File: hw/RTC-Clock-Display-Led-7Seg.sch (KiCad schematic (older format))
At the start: 86 parts, among them IC1 STM8S003F3P, J1 BARREL_JACK, J4 CONN_01X04, Q1 A1015, Q10 C1815, Q2 A1015, Q3 A1015, Q4 A1015, Q5 C1815, Q6 C1815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

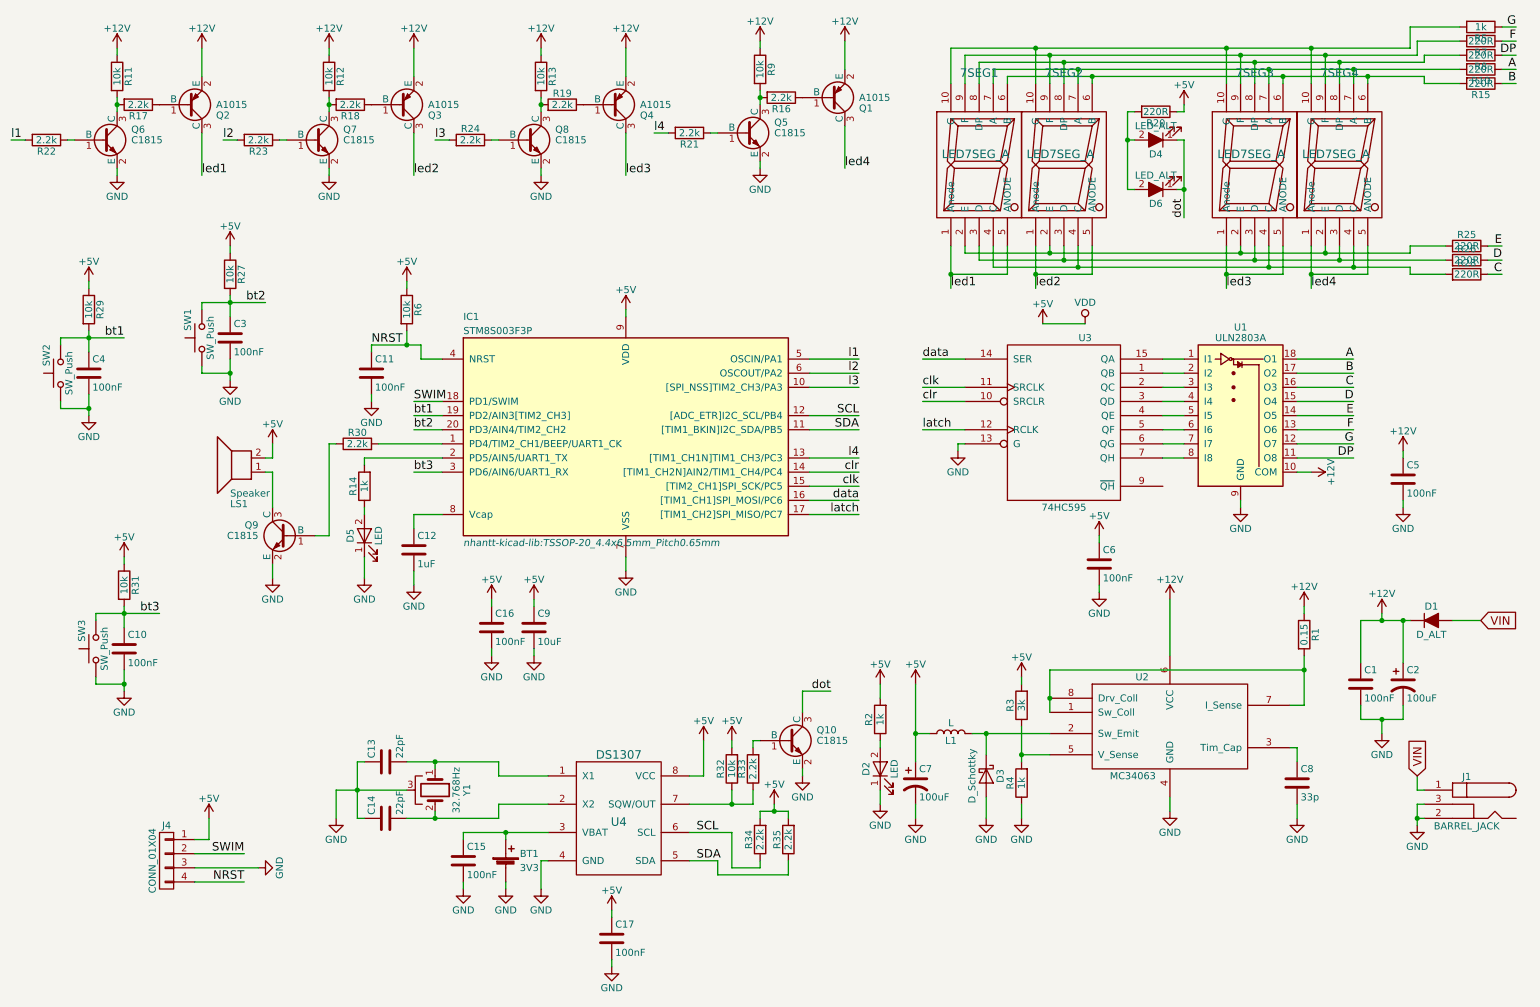
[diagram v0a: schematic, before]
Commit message: add lib layout
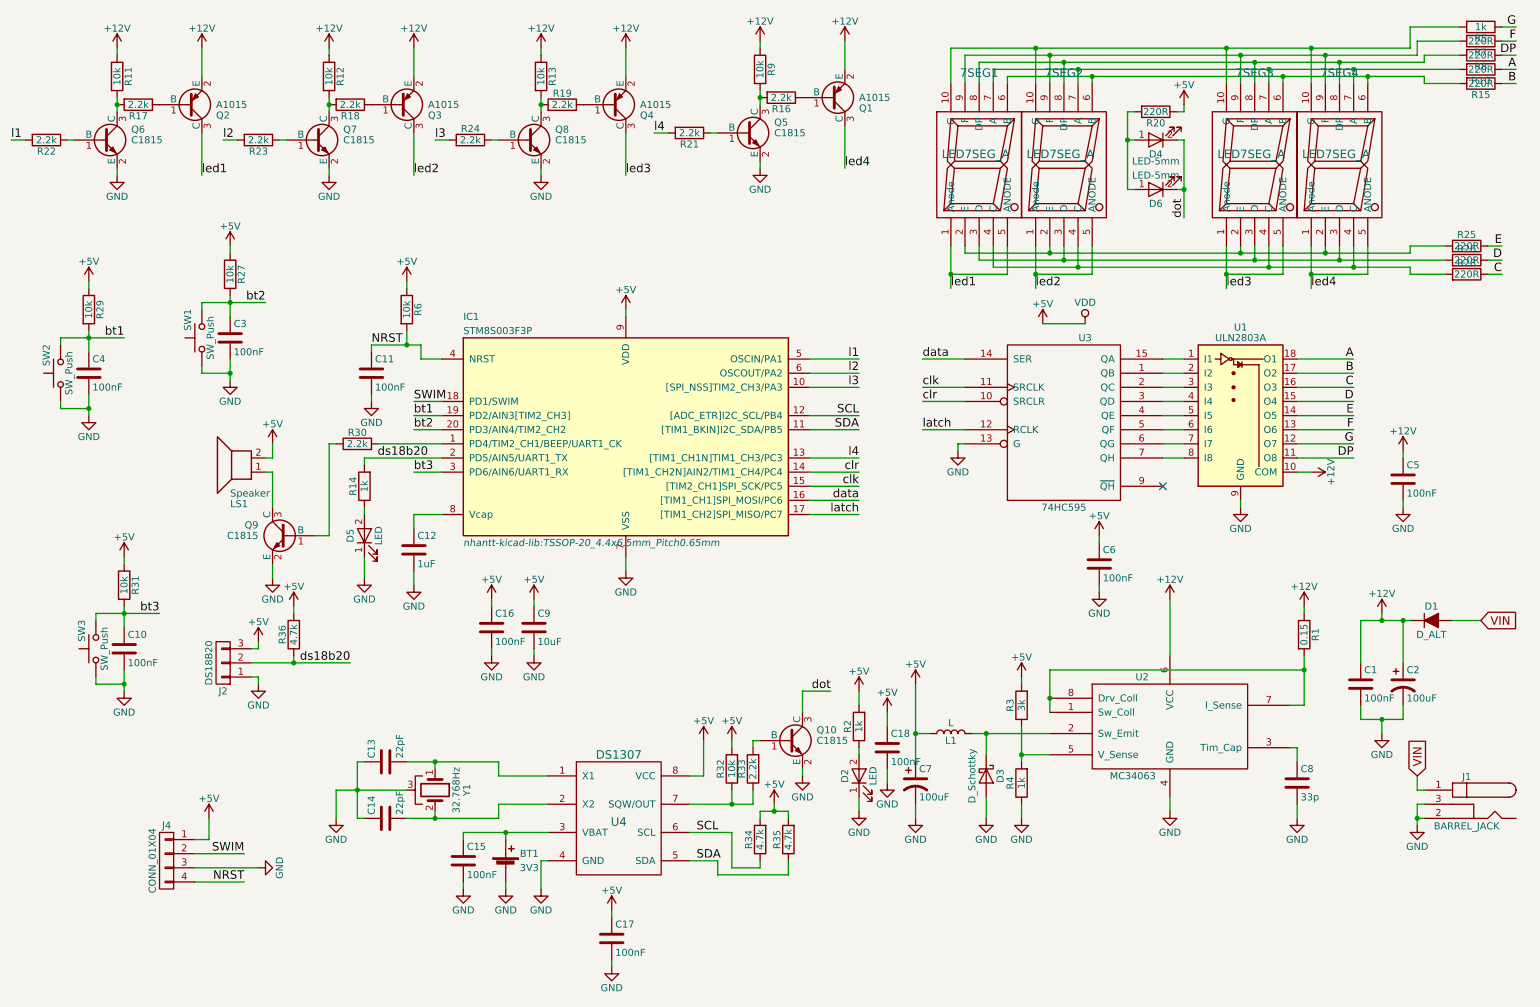
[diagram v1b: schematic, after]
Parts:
- removed D4, D6: LED_ALT, symbol LED_ALT
- added C18: 100nF, Capacitors_SMD:C_0805_HandSoldering, symbol C
- added D4, D6: LED-5mm, LEDs:LED_D5.0mm, symbol LED-5mm
- added J2: DS18B20, TO_SOT_Packages_THT:TO-92_Inline_Wide, symbol CONN_01X03
- added R36: 4.7k, Resistors_SMD:R_0805_HandSoldering, symbol R
- 7SEG1, 7SEG2, 7SEG3, 7SEG4: footprint (none) -> nhantt-kicad-lib:LED-7SEG-23101BX
- J4: footprint Pin_Headers:Pin_Header_Straight_1x04_Pitch2.54mm -> nhantt-kicad-lib:Header-4pin-2.54
- LS1: footprint (none) -> Buzzers_Beepers:Buzzer_12x9.5RM7.6
- Q1, Q2, Q3, Q4: footprint TO_SOT_Packages_THT:TO-92_Molded_Narrow -> nhantt-kicad-lib:SOT-23
- R34, R35: value 2.2k -> 4.7k
- U1: footprint (none) -> nhantt-kicad-lib:SOIC-18W_7.5x11.6mm_Pitch1.27mm
- U3: footprint (none) -> nhantt-kicad-lib:SOIC-16W_5.3x10.2mm_Pitch1.27mm
- Y1: footprint nhantt-kicad-lib:Crystal_Round_Horizontal_3mm -> nhantt-kicad-lib:Crystal_Round_Horizontal_3mm_smd
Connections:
- net +5V: now also C18.1, J2.3 (P3), R36.2
- net GND: now also C18.2, J2.1 (P1)
- net dot: now also D4.2 (K), D6.2 (K)
- net ds18b20: now reaches IC1.2 (PD5/AIN5/UART1_TX), R14.2
- net ds18b20: now also J2.2 (P2), R36.1
- net at R20.2: now also D4.1 (A), D6.1 (A)
- no-connect marks 0 -> 1
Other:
- moved on the sheet: D2, R2

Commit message: complete layout
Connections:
- net VCC is gone; now on net +5V: U3.16 (VCC)
- net A: now also U1.11 (O8); no longer U1.18 (O1)
- net B: now also U1.12 (O7); no longer U1.17 (O2)
- net C: now also U1.13 (O6); no longer U1.16 (O3)
- net D: now also U1.14 (O5); no longer U1.15 (O4)
- net DP: now also U1.18 (O1); no longer U1.11 (O8)
- net E: now also U1.15 (O4); no longer U1.14 (O5)
- net F: now also U1.16 (O3); no longer U1.13 (O6)
- net G: now also U1.17 (O2); no longer U1.12 (O7)
- net bt1: now also IC1.20 (PD3/AIN4/TIM2_CH2); no longer IC1.19 (PD2/AIN3[TIM2_CH3])
- net bt2: now also IC1.3 (PD6/AIN6/UART1_RX); no longer IC1.20 (PD3/AIN4/TIM2_CH2)
- net bt3: now also IC1.19 (PD2/AIN3[TIM2_CH3]); no longer IC1.3 (PD6/AIN6/UART1_RX)
- net l1: now also IC1.10 ([SPI_NSS]TIM2_CH3/PA3); no longer IC1.5 (OSCIN/PA1)
- net l3: now also IC1.5 (OSCIN/PA1); no longer IC1.10 ([SPI_NSS]TIM2_CH3/PA3)
- net QA: now reaches U3.15 (QA)
- net QA: now also U1.8 (I8); no longer U1.1 (I1)
- net QB: now reaches U3.1 (QB)
- net QB: now also U1.7 (I7); no longer U1.2 (I2)
- net QC: now reaches U3.2 (QC)
- net QC: now also U1.6 (I6); no longer U1.3 (I3)
- net QD: now reaches U3.3 (QD)
- net QD: now also U1.5 (I5); no longer U1.4 (I4)
- net QE: now reaches U3.4 (QE)
- net QE: now also U1.4 (I4); no longer U1.5 (I5)
- net QF: now reaches U3.5 (QF)
- net QF: now also U1.3 (I3); no longer U1.6 (I6)
- net QG: now reaches U3.6 (QG)
- net QG: now also U1.2 (I2); no longer U1.7 (I7)
- net QH: now reaches U3.7 (QH)
- net QH: now also U1.1 (I1); no longer U1.8 (I8)
- net at C13.2, U4.1 (X1): now also Y1.2; no longer Y1.1
- net at C14.2, U4.2 (X2): now also Y1.1; no longer Y1.2
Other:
- moved on the sheet: C5, U1
